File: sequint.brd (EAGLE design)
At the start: 70 x 80 mm, 66 parts, among them IC1 STM32F10XCXT6, Q1 MOSFET-NCHANNELSMD, Q2 MOSFET-NCHANNELSMD, Q3 MOSFET-NCHANNELSMD, Q4 MOSFET-NCHANNELSMD, Q5 16MHz, U1 LSM330DLCTRLGA, U2 MCP73831, U4 NRF24L01SMD

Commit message: Vias around USB
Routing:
- net GND: vias 24 -> 28
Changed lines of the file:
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@@
 <via x="26.416" y="57.15" extent="1-16" drill="0.3302"/>
 <via x="16.383" y="42.545" extent="1-16" drill="0.3302"/>
+<via x="21.696" y="69.678" extent="1-16" drill="0.3302"/>
+<via x="17.759" y="78.568" extent="1-16" drill="0.3302"/>
+<via x="31.983" y="78.568" extent="1-16" drill="0.3302"/>
+<via x="29.443" y="70.186" extent="1-16" drill="0.3302"/>
 </signal>
 <signal name="3.3V">

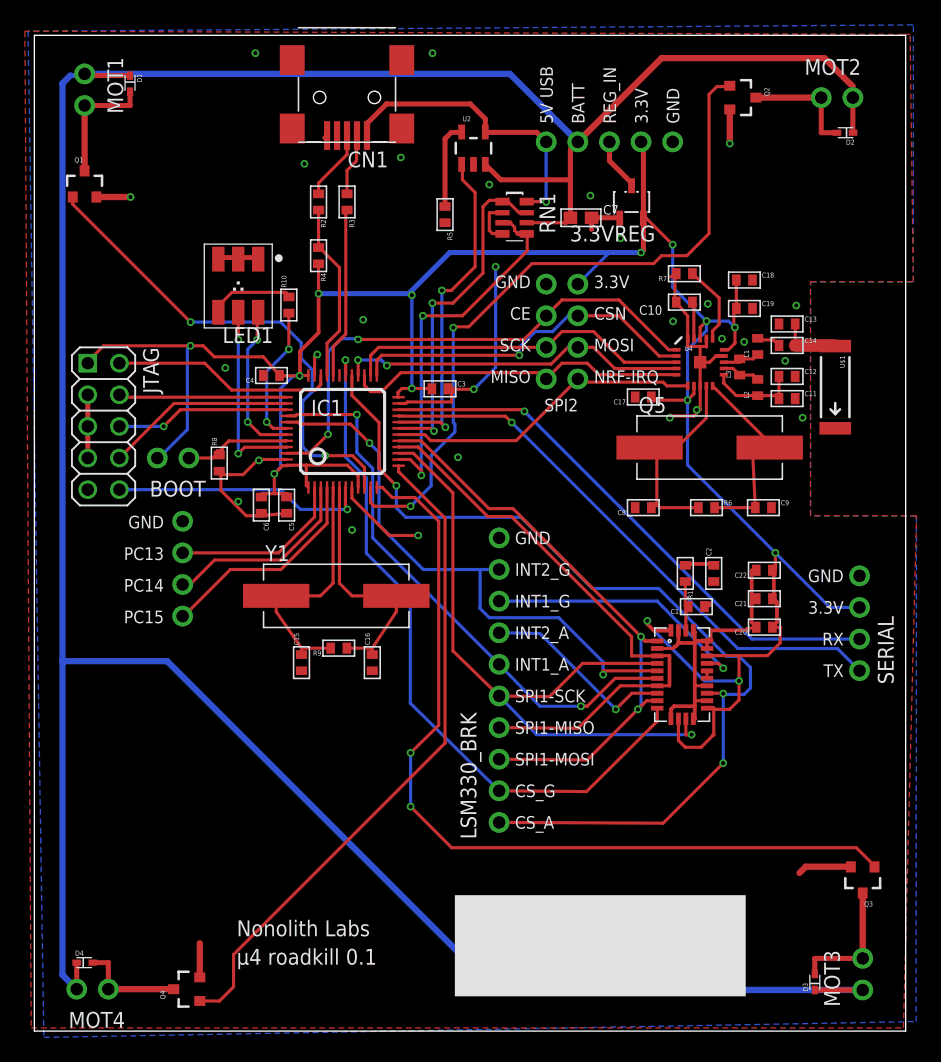
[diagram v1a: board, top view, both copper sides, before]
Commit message: Add servo headers
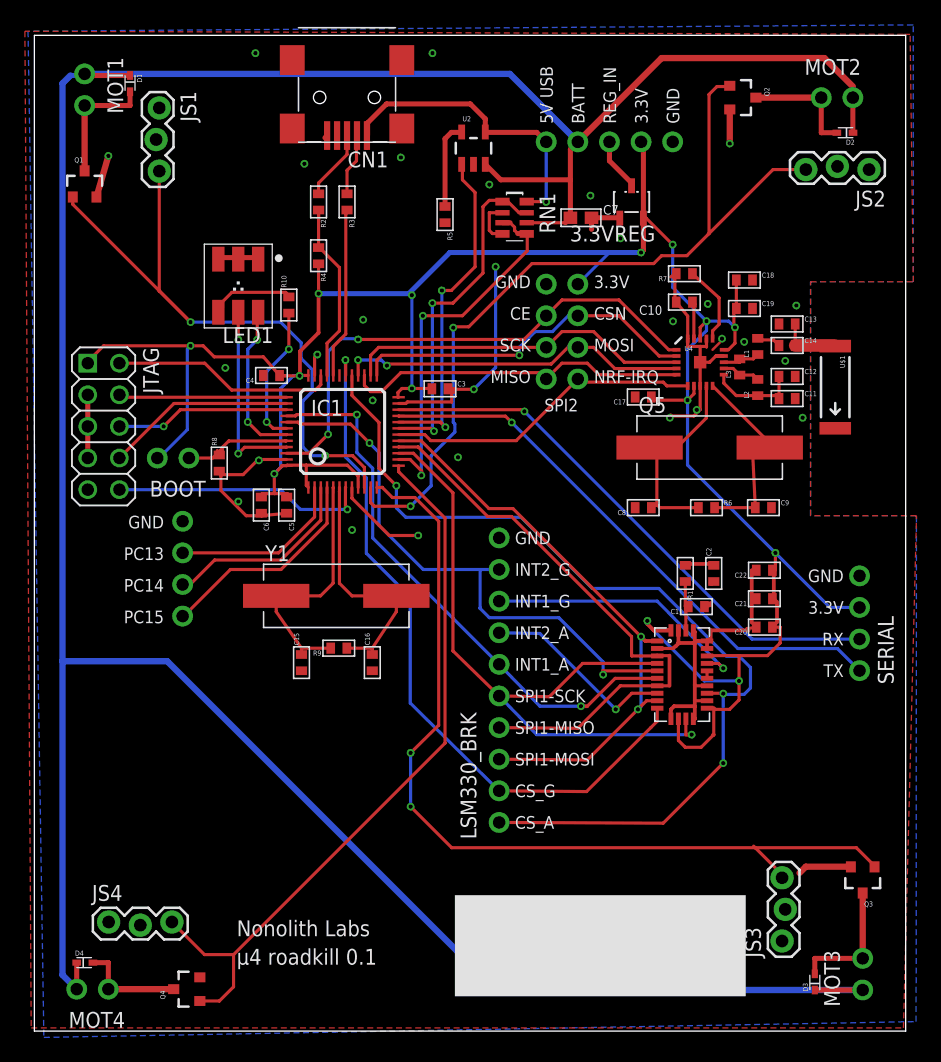
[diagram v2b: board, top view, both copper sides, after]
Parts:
- added JS1, JS2, JS3, JS4: (no value), SparkFun:1X03_LOCK
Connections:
- net GND: now also JS1.1, JS2.1, JS3.1, JS4.1
- net TMR2-CH1: now also JS1.3
- net TMR2-CH2: now also JS2.3
- net TMR2-CH3: now also JS3.3
- net TMR2-CH4: now also JS4.3
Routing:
- net TMR2-CH1: track 39.9 -> 53.1 mm
- net TMR2-CH2: track 57.5 -> 67.4 mm
- net TMR2-CH4: track 53.6 -> 59.7 mm
- net TMR2-CH3: track 69.3 -> 72.8 mm
- net GND: track 125.2 -> 124.1 mm, vias 28 -> 29
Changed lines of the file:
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@@
 </variantdefs>
 <classes>
-<class number="0" name="default" width="0.254" drill="0">
+<class number="0" name="default" width="0.2032" drill="0">
 <clearance class="0" value="0.1778"/>
 </class>
@@
 <element name="D3" library="SparkFun-DiscreteSemi" package="SOD523" value="" x="62.7" y="3.9" rot="R90"/>
 <element name="D4" library="SparkFun-DiscreteSemi" package="SOD523" value="" x="4" y="5.5"/>
+<element name="JS1" library="SparkFun" package="1X03_LOCK" value="" x="9.906" y="74.168" rot="R270"/>
+<element name="JS2" library="SparkFun" package="1X03_LOCK" value="" x="67.056" y="69.342" rot="R180"/>
+<element name="JS3" library="SparkFun" package="1X03_LOCK" value="" x="60.198" y="7.239" rot="R90"/>
+<element name="JS4" library="SparkFun" package="1X03_LOCK" value="" x="5.969" y="8.636"/>
 </elements>
 <signals>
@@
 <contactref element="Q3" pad="2"/>
 <contactref element="Q4" pad="2"/>
-<wire x1="4.986" y1="67.011" x2="7.726" y2="67.011" width="0.508" layer="1"/>
+<wire x1="4.986" y1="67.011" x2="5.948" y2="70.313" width="0.508" layer="1"/>
 <wire x1="55.868" y1="74.046" x2="55.868" y2="71.306" width="0.508" layer="1"/>
-<wire x1="13.291" y1="7.058" x2="13.291" y2="4.318" width="0.508" layer="1"/>
-<via x="7.726" y="67.011" extent="1-16" drill="0.3302"/>
+<via x="5.948" y="70.313" extent="1-16" drill="0.3302"/>
 <via x="55.868" y="71.306" extent="1-16" drill="0.3302"/>
 <wire x1="22.5124" y1="52.6736" x2="22.5124" y2="54.1024" width="0.254" layer="1"/>
@@
 <via x="31.983" y="78.568" extent="1-16" drill="0.3302"/>
 <via x="29.443" y="70.186" extent="1-16" drill="0.3302"/>
+<via x="27.178" y="50.673" extent="1-16" drill="0.3302"/>
+<wire x1="55.118" y1="55.372" x2="54.483" y2="54.737" width="0.2032" layer="1"/>
+<contactref element="JS1" pad="1"/>
+<contactref element="JS2" pad="1"/>
+<contactref element="JS3" pad="1"/>
+<contactref element="JS4" pad="1"/>
 </signal>
 <signal name="3.3V">
@@
 <wire x1="29.2624" y1="44.9436" x2="29.2624" y2="45.4236" width="0.254" layer="1"/>
 <wire x1="32.992" y1="23.135" x2="16.002" y2="6.145" width="0.254" layer="1"/>
+<contactref element="JS4" pad="3"/>
+<wire x1="16.002" y1="6.145" x2="13.667" y2="6.145" width="0.254" layer="1"/>
+<wire x1="13.667" y1="6.145" x2="11.049" y2="8.763" width="0.254" layer="1"/>
 </signal>
 <signal name="TMR2-CH1">
@@
 <via x="23.368" y="46.228" extent="1-16" drill="0.3302"/>
 <wire x1="23.368" y1="46.228" x2="25.565" y2="46.228" width="0.254" layer="1"/>
+<contactref element="JS1" pad="3"/>
+<wire x1="10.033" y1="69.088" x2="10.033" y2="59.436" width="0.254" layer="1"/>
+<wire x1="10.033" y1="59.436" x2="10.071" y2="59.436" width="0.254" layer="1"/>
+<wire x1="10.071" y1="59.436" x2="12.545" y2="56.962" width="0.254" layer="1"/>
 </signal>
 <signal name="TMR2-CH2">
@@
 <wire x1="49.756" y1="61.661" x2="50.391" y2="62.296" width="0.254" layer="1"/>
 <wire x1="50.391" y1="62.296" x2="52.423" y2="62.296" width="0.254" layer="1"/>
-<wire x1="52.423" y1="62.296" x2="54.201" y2="64.074" width="0.254" layer="1"/>
+<wire x1="52.423" y1="62.296" x2="54.1185" y2="63.9915" width="0.254" layer="1"/>
+<wire x1="54.1185" y1="63.9915" x2="54.201" y2="64.074" width="0.254" layer="1"/>
 <wire x1="54.201" y1="64.074" x2="54.201" y2="75.25" width="0.254" layer="1"/>
 <wire x1="54.201" y1="75.25" x2="54.836" y2="75.885" width="0.254" layer="1"/>
@@
 <wire x1="27.305" y1="42.164" x2="30.226" y2="42.164" width="0.254" layer="1"/>
 <via x="30.226" y="42.164" extent="1-16" drill="0.3302"/>
+<contactref element="JS2" pad="3"/>
+<wire x1="61.976" y1="69.215" x2="59.342" y2="69.215" width="0.254" layer="1"/>
+<wire x1="59.342" y1="69.215" x2="54.201" y2="64.074" width="0.254" layer="1"/>
 </signal>
 <signal name="TMR2-CH3">
@@
 <wire x1="67.31" y1="13.38" x2="67.31" y2="13.462" width="0.254" layer="1"/>
 <wire x1="67.31" y1="13.462" x2="66.04" y2="14.732" width="0.254" layer="1"/>
-<wire x1="66.04" y1="14.732" x2="33.528" y2="14.732" width="0.254" layer="1"/>
+<wire x1="66.04" y1="14.732" x2="57.912" y2="14.732" width="0.254" layer="1"/>
+<wire x1="57.912" y1="14.732" x2="33.528" y2="14.732" width="0.254" layer="1"/>
 <wire x1="33.528" y1="14.732" x2="30.226" y2="18.034" width="0.254" layer="1"/>
 <via x="30.226" y="18.034" extent="1-16" drill="0.3302"/>
 <wire x1="30.226" y1="18.034" x2="30.226" y2="22.352" width="0.254" layer="16"/>
+<contactref element="JS3" pad="3"/>
+<wire x1="60.071" y1="12.319" x2="60.071" y2="12.573" width="0.254" layer="1"/>
+<wire x1="57.912" y1="14.732" x2="57.785" y2="14.859" width="0.254" layer="1"/>
+<wire x1="60.071" y1="12.573" x2="57.912" y2="14.732" width="0.254" layer="1"/>
 </signal>
 <signal name="SPI2-NSS">

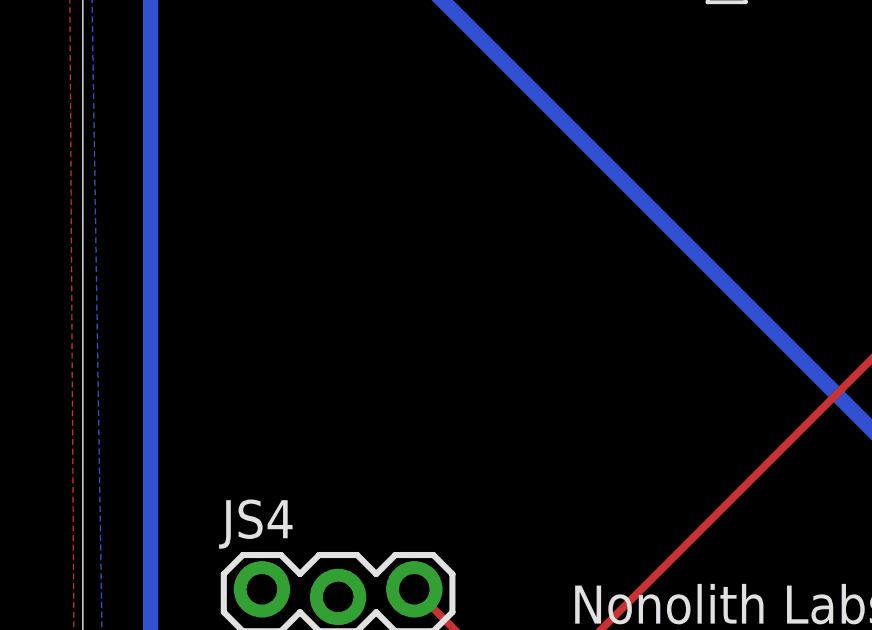
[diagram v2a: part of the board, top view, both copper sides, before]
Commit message: Add test motor footprint
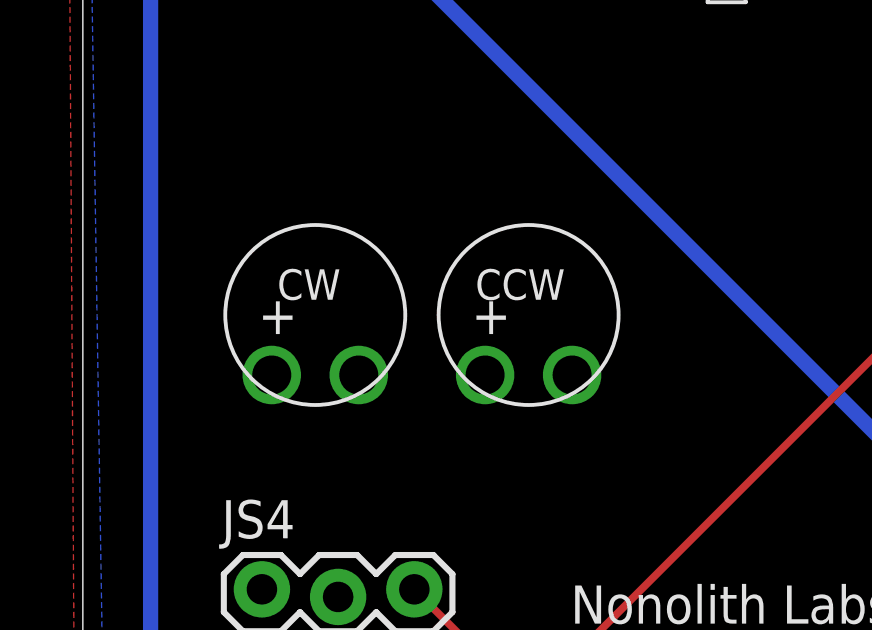
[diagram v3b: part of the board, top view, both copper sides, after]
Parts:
- added U$6: MOT_RICCW, nonolith:MOT_RIC_BM_CW
- added U$7: MOT_RICCCW, nonolith:MOT_RIC_BM_CCW
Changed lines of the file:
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@@
 <element name="JS3" library="SparkFun" package="1X03_LOCK" value="" x="60.198" y="7.239" rot="R90"/>
 <element name="JS4" library="SparkFun" package="1X03_LOCK" value="" x="5.969" y="8.636"/>
+<element name="U$6" library="nonolith" package="MOT_RIC_BM_CW" value="MOT_RICCW" x="7.747" y="17.907"/>
+<element name="U$7" library="nonolith" package="MOT_RIC_BM_CCW" value="MOT_RICCCW" x="14.859" y="17.907"/>
 </elements>
 <signals>

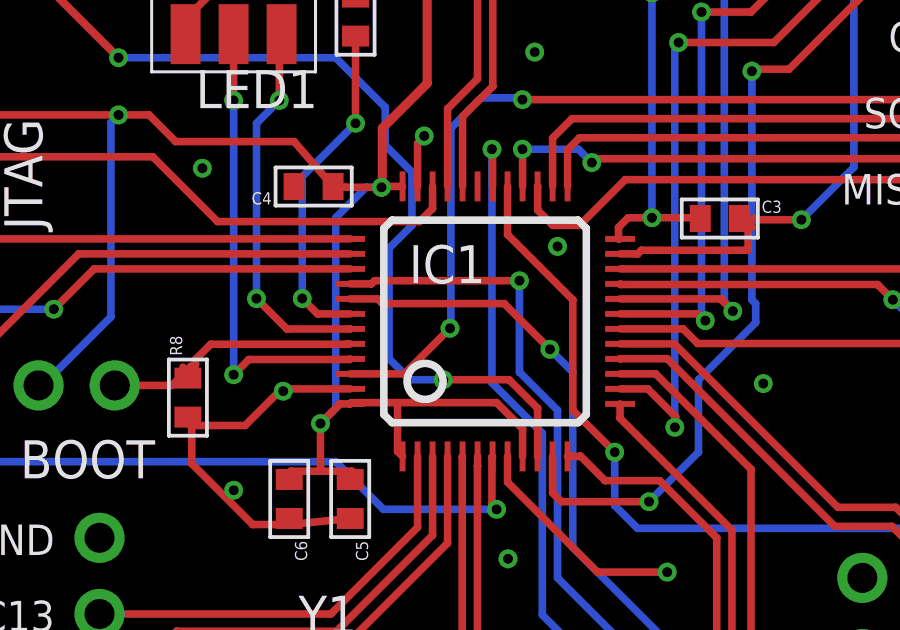
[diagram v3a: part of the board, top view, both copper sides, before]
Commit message: Fix routing on two STM32 pins; update lbr
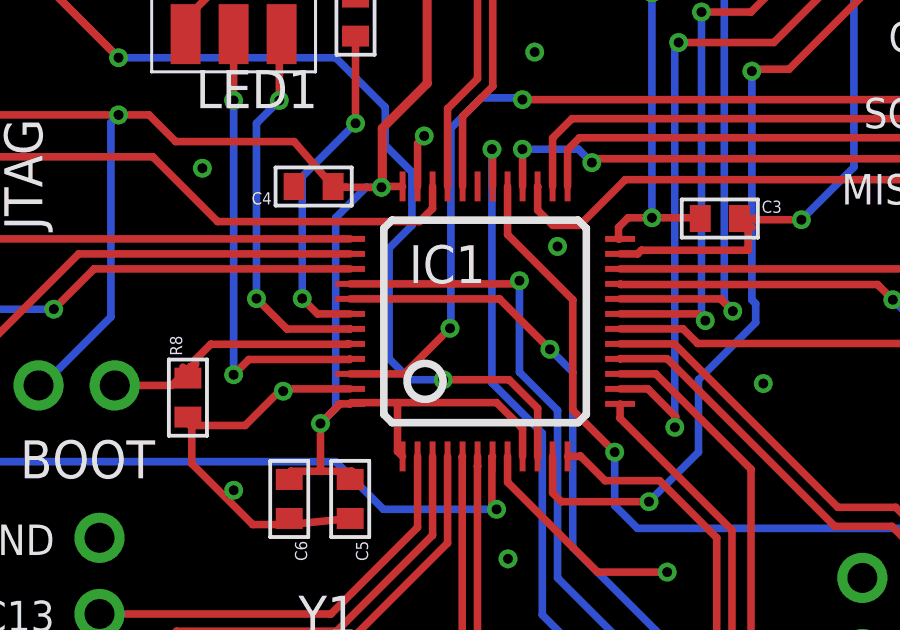
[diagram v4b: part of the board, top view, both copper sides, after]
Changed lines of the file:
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@@
 <wire x1="43.914" y1="26.101" x2="40.612" y2="26.101" width="0.254" layer="16"/>
 <wire x1="40.612" y1="26.101" x2="37.338" y2="29.464" width="0.254" layer="16"/>
-<wire x1="20.2624" y1="49.4236" x2="20.9756" y2="49.4236" width="0.254" layer="1"/>
-<wire x1="20.9756" y1="49.4236" x2="21.082" y2="49.53" width="0.254" layer="1"/>
-<wire x1="21.082" y1="49.53" x2="25.908" y2="49.53" width="0.254" layer="1"/>
 <via x="25.908" y="49.53" extent="1-16" drill="0.3302"/>
 <wire x1="25.908" y1="49.53" x2="25.908" y2="46.482" width="0.254" layer="16"/>
@@
 <wire x1="27.178" y1="39.624" x2="37.338" y2="29.464" width="0.254" layer="16"/>
 <wire x1="50.042" y1="28.341" x2="46.662" y2="28.341" width="0.254" layer="1"/>
+<wire x1="20.2624" y1="49.4236" x2="25.908" y2="49.4236" width="0.254" layer="1"/>
+<wire x1="25.908" y1="49.4236" x2="25.908" y2="49.53" width="0.254" layer="1"/>
 </signal>
 <signal name="GND">
@@
 <contactref element="JS3" pad="1"/>
 <contactref element="JS4" pad="1"/>
+<wire x1="54.042" y1="27.741" x2="54.042" y2="28.341" width="0" layer="19" extent="1-1"/>
 </signal>
 <signal name="3.3V">
@@
 <wire x1="42.136" y1="33.213" x2="36.548" y2="33.213" width="0.254" layer="16"/>
 <wire x1="36.548" y1="33.213" x2="35.786" y2="33.975" width="0.254" layer="16"/>
-<wire x1="20.2624" y1="48.9236" x2="21.1804" y2="48.9236" width="0.254" layer="1"/>
-<wire x1="21.336" y1="48.768" x2="25.4" y2="48.768" width="0.254" layer="1"/>
-<wire x1="25.4" y1="48.768" x2="26.924" y2="47.244" width="0.254" layer="1"/>
+<wire x1="25.2444" y1="48.9236" x2="26.924" y2="47.244" width="0.254" layer="1"/>
 <via x="26.924" y="47.244" extent="1-16" drill="0.3302"/>
 <wire x1="26.924" y1="47.244" x2="27.686" y2="46.482" width="0.254" layer="16"/>
@@
 <wire x1="37.084" y1="37.084" x2="37.145" y2="37.023" width="0.254" layer="16"/>
 <wire x1="37.145" y1="37.023" x2="37.338" y2="37.084" width="0.254" layer="16"/>
-<wire x1="21.1804" y1="48.9236" x2="21.336" y2="48.768" width="0.254" layer="1"/>
 <wire x1="50.042" y1="28.941" x2="45.692" y2="28.941" width="0.254" layer="1"/>
+<wire x1="20.2624" y1="48.9236" x2="25.2444" y2="48.9236" width="0.254" layer="1"/>
 </signal>
 <signal name="N$2">
